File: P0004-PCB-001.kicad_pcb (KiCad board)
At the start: 2 copper layers, 63.5 x 38.5 mm, 58 parts, among them CN1 Molex 105057-0001, CN2 104031-0811, CN3 Liansheng PH--00603, CN4 Samtec FTSH-107-01-L-DV-K, CN5 M20-9990346, SW1 Khon TSB06331-090D332DA-R0500, SW2 Khon TSB06331-090D332DA-R0500, SW3 Khon TSB06331-090D332DA-R0500, SW4 Khon TSB06331-090D332DA-R0500, U1 W5500, U2 STM32H743VIT6, U3 Microchip 24AA256UIDT-I/ST, U4 INA3221AIRGV, U5 TMP102AIDRL, U6 TI LMR54410DBV

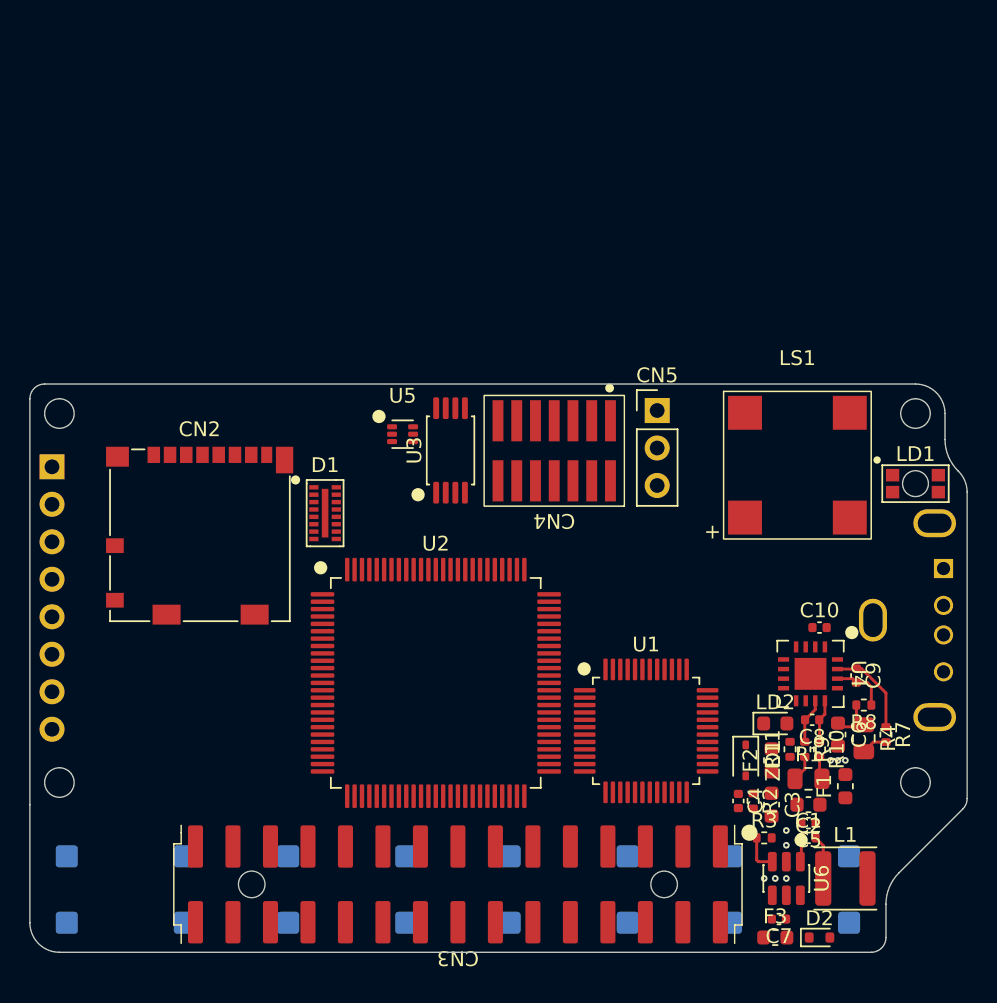
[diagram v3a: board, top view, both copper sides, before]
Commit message: added ethernet phy
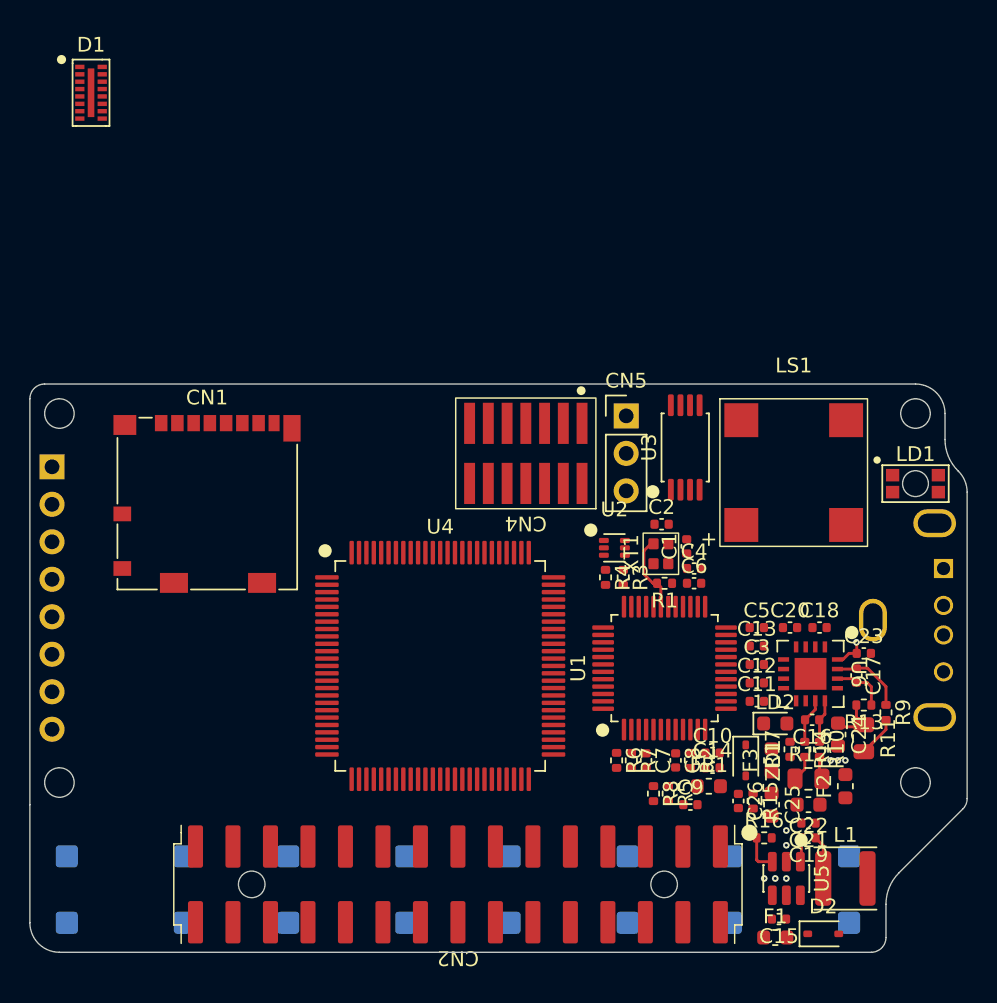
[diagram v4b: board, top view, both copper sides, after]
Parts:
- added C1: 18p, Capacitor_WUT:C_0402_1005Metric, F.Cu at (188.5, 96.5)
- added C10: 100n, Capacitor_WUT:C_0402_1005Metric, F.Cu at (190.2, 110.5)
- added C11: 100n, Capacitor_WUT:C_0402_1005Metric, F.Cu at (193.2, 107.0)
- added C12: 100n, Capacitor_WUT:C_0402_1005Metric, F.Cu at (193.2, 105.8)
- added C13: 100n, Capacitor_WUT:C_0402_1005Metric, F.Cu at (193.2, 103.2)
- added C14: 4u7, Capacitor_WUT:C_0402_1005Metric, F.Cu at (190.2, 111.5)
- added C19: 100n, Capacitor_WUT:C_0402_1005Metric, F.Cu at (196.8, 116.2)
- added C2: 18p, Capacitor_WUT:C_0402_1005Metric, F.Cu at (186.8, 95.0)
- added C20: 100n, Capacitor_WUT:C_0402_1005Metric, F.Cu at (195.5, 102.0)
- added C23: 100n, Capacitor_WUT:C_0402_1005Metric, F.Cu at (200.5, 103.8)
- added C3: 4u7, Capacitor_WUT:C_0402_1005Metric, F.Cu at (193.2, 104.5)
- added C4: 4u7, Capacitor_WUT:C_0402_1005Metric, F.Cu at (189.0, 98.0)
- added C5: 100n, Capacitor_WUT:C_0402_1005Metric, F.Cu at (193.2, 102.0)
- added C6: 100n, Capacitor_WUT:C_0402_1005Metric, F.Cu at (189.0, 99.0)
- added C7: 100n, Capacitor_WUT:C_0402_1005Metric, F.Cu at (185.8, 111.0)
- added C8: 100n, Capacitor_WUT:C_0402_1005Metric, F.Cu at (187.8, 111.0)
- added FB1: 600R, Inductor_SMD:L_0603_1608Metric, F.Cu at (190.0, 112.8)
- added R1: 1M0, Resistor_WUT:R_0402_1005Metric, F.Cu at (187.0, 99.0)
- added R2: 12k4, Resistor_WUT:R_0402_1005Metric, F.Cu at (188.8, 111.0)
- added R3: 10k, Resistor_WUT:R_0402_1005Metric, F.Cu at (184.2, 98.6)
- added R4: 10k, Resistor_WUT:R_0402_1005Metric, F.Cu at (183.0, 98.6)
- added R5: 49R9, Resistor_WUT:R_0402_1005Metric, F.Cu at (187.2, 113.2)
- added R6: 3R3, Resistor_WUT:R_0402_1005Metric, F.Cu at (183.8, 111.0)
- added R7: 3R3, Resistor_WUT:R_0402_1005Metric, F.Cu at (184.8, 111.0)
- added R8: 49R9, Resistor_WUT:R_0402_1005Metric, F.Cu at (186.2, 113.2)
- added XT1: 25MHz, Crystal_WUT:Murata_XRCGB, F.Cu at (186.8, 97.0)
- D2: footprint Diode_SMD:D_SOD-523 -> Diode_SMD:D_SOD-323
- moved D1 32.6 mm to (148.1, 65.8)
- moved U2 16.3 mm to (183.6, 96.6)
- moved U3 15.9 mm to (188.4, 89.8)
- moved C9 8.31 mm to (188.8, 114.0)
- moved U1 4.43 mm to (187.0, 104.8), turned to 90 degrees
- moved CN1 2.21 mm to (156.0, 93.6)
- moved CN5 2.13 mm to (184.4, 87.7)
- moved CN4 1.93 mm to (177.6, 90.2)
- moved R9 1.50 mm to (202.0, 107.8)
- moved U4 1.19 mm to (171.8, 104.6)
- moved LS1 0.56 mm to (195.8, 91.5)
- moved D2 0.35 mm to (197.8, 122.8)
- renumbered C7 to C15, C8 to C16, C9 to C17, C10 to C18, C5 to C21, C2 to C22, C6 to C24, C3 to C25, C4 to C26, C1 to C9, CN2 to CN1, CN3 to CN2, CN1 to CN3, F3 to F1, F1 to F2, F2 to F3, H5 to H1, H4 to H10, H8 to H11, H9 to H2, H1 to H3, H6 to H4, H10 to H5, H2 to H6, H3 to H7, H7 to H8, H11 to H9, R4 to R11, R1 to R12, R8 to R13, R9 to R14, R2 to R15, R3 to R16, R11 to R17, R7 to R9, U5 to U2, U2 to U4, U6 to U5, U4 to U6
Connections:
- net Net-(U1-AVDD-Pad11) renamed /Ethernet/PHY_VDDA
- net Net-(U4-IN3+) renamed /Power Supplies/12V_AUX_SENSE_P
- net Net-(U4-IN3-) renamed /Power Supplies/12V_AUX_SENSE_N
- C26 pad 2: Net-(U6-FB) -> 0V
- C9 pad 1: Net-(U6-CB) -> Net-(C9-Pad1)
- C9 pad 2: /Power Supplies/SW -> 0V
- R15 pad 2: Net-(U6-FB) -> Net-(U5-FB)
- R16 pad 1: Net-(U6-FB) -> Net-(U5-FB)
- U1 pad 1: unconnected-(U1-TXN-Pad1) -> Net-(U1-TXN)
- U1 pad 10: unconnected-(U1-EXRES1-Pad10) -> Net-(U1-EXRES1)
- U1 pad 14: Net-(U1-AGND-Pad14) -> 0V
- U1 pad 16: Net-(U1-AGND-Pad14) -> 0V
- U1 pad 19: Net-(U1-AGND-Pad14) -> 0V
- U1 pad 2: unconnected-(U1-TXP-Pad2) -> Net-(U1-TXP)
- U1 pad 20: unconnected-(U1-TOCAP-Pad20) -> Net-(U1-TOCAP)
- U1 pad 22: unconnected-(U1-1V2O-Pad22) -> Net-(U1-1V2O)
- U1 pad 23: unconnected-(U1-RSVD-Pad23) -> 0V
- U1 pad 25: unconnected-(U1-LINKLED-Pad25) -> /Ethernet/~{ETH_LINK_OD}
- U1 pad 27: unconnected-(U1-ACTLED-Pad27) -> /Ethernet/~{ETH_ACT_OD}
- U1 pad 28: unconnected-(U1-VDD-Pad28) -> 3V3
- U1 pad 29: unconnected-(U1-GND-Pad29) -> 0V
- U1 pad 3: Net-(U1-AGND-Pad14) -> 0V
- U1 pad 30: unconnected-(U1-XI/CLKIN-Pad30) -> Net-(U1-XI/CLKIN)
- U1 pad 31: unconnected-(U1-XO-Pad31) -> Net-(U1-XO)
- U1 pad 32: unconnected-(U1-~{SCS}-Pad32) -> /Ethernet/~{CS}
- U1 pad 33: unconnected-(U1-SCLK-Pad33) -> /Ethernet/SCLK
- U1 pad 34: unconnected-(U1-MISO-Pad34) -> /Ethernet/MISO
- U1 pad 35: unconnected-(U1-MOSI-Pad35) -> /Ethernet/MOSI
- U1 pad 36: unconnected-(U1-~{INT}-Pad36) -> /Ethernet/~{ETH_PHY_INT}
- U1 pad 37: unconnected-(U1-~{RST}-Pad37) -> /Ethernet/~{ETH_PHY_RST}
- U1 pad 43: unconnected-(U1-PMODE2-Pad43) -> 3V3
- U1 pad 44: unconnected-(U1-PMODE1-Pad44) -> 3V3
- U1 pad 45: unconnected-(U1-PMODE0-Pad45) -> 3V3
- U1 pad 48: Net-(U1-AGND-Pad14) -> 0V
- U1 pad 5: unconnected-(U1-RXN-Pad5) -> /Ethernet/ETH_RX_P
- U1 pad 6: unconnected-(U1-RXP-Pad6) -> /Ethernet/ETH_RX_N
- U1 pad 9: Net-(U1-AGND-Pad14) -> 0V
- U4 pad 10: unconnected-(U2-VSS-Pad10) -> 0V
- U4 pad 19: unconnected-(U2-VSSA-Pad19) -> 0V
- U4 pad 26: unconnected-(U2-VSS-Pad26) -> 0V
- U4 pad 49: unconnected-(U2-VSS-Pad49) -> 0V
- U4 pad 74: unconnected-(U2-VSS-Pad74) -> 0V
- U4 pad 99: unconnected-(U2-VSS-Pad99) -> 0V
- U5 pad 1: Net-(U6-CB) -> Net-(U5-CB)
- U5 pad 3: Net-(U6-FB) -> Net-(U5-FB)
- U6 pad 16: unconnected-(U4-VPU-Pad16) -> 3V3
- U6 pad 4: unconnected-(U4-VS-Pad4) -> 3V3
- U6 pad 6: unconnected-(U4-SCL-Pad6) -> /Power Supplies/SCL
- U6 pad 7: unconnected-(U4-SDA-Pad7) -> /Power Supplies/SDA
- U6 pad 9: unconnected-(U4-CRITICAL-Pad9) -> /Power Supplies/~{PWR_FAULT_OD}
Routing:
- net Net-(U1-XO): track 0.00 -> 5.27 mm
- net Net-(U6-FB): track 2.60 -> 0.00 mm
- net Net-(U5-FB): track 0.00 -> 2.60 mm
- net 3V3: track 0.00 -> 2.24 mm, vias 0 -> 1
- net Net-(F2-Pad2): track 1.77 -> 3.70 mm
- net Net-(U6-CB): track 1.74 -> 0.00 mm
- net Net-(U5-CB): track 0.00 -> 1.74 mm
- net /Power Supplies/3V3_EXPANSION_SENSE_P: track 6.30 -> 5.07 mm

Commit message: started on mcu pinout
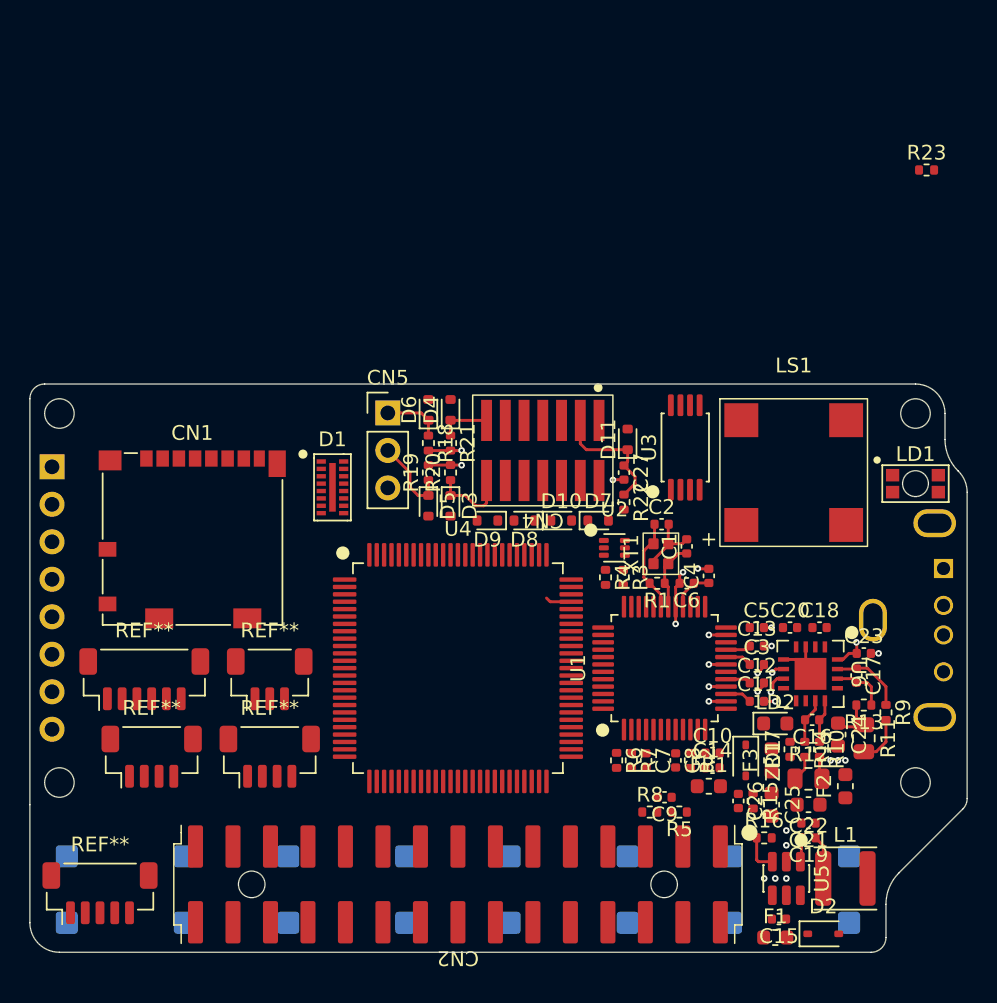
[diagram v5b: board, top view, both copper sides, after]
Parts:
- added C27: 100n, Capacitor_WUT:C_0402_1005Metric, F.Cu at (184.2, 91.5)
- added D10: 3V3, Diode_SMD:D_SOD-523, F.Cu at (180.0, 94.8)
- added D11: 3V3, Diode_SMD:D_SOD-523, F.Cu at (184.5, 89.2)
- added D3: 3V3, Diode_SMD:D_SOD-523, F.Cu at (172.5, 93.8)
- added D4: 3V3, Diode_SMD:D_SOD-523, F.Cu at (172.5, 87.2)
- added D5: 3V3, Diode_SMD:D_SOD-523, F.Cu at (171.0, 93.8)
- added D6: 3V3, Diode_SMD:D_SOD-523, F.Cu at (171.0, 87.2)
- added D7: 3V3, Diode_SMD:D_SOD-523, F.Cu at (182.5, 94.8)
- added D8: 3V3, Diode_SMD:D_SOD-523, F.Cu at (177.5, 94.8)
- added D9: 3V3, Diode_SMD:D_SOD-523, F.Cu at (175.0, 94.8)
- added R18: 100R, Resistor_WUT:R_0402_1005Metric, F.Cu at (171.0, 89.5)
- added R19: 100R, Resistor_WUT:R_0402_1005Metric, F.Cu at (171.0, 91.5)
- added R20: 100R, Resistor_WUT:R_0402_1005Metric, F.Cu at (172.5, 91.5)
- added R21: 100R, Resistor_WUT:R_0402_1005Metric, F.Cu at (172.5, 89.5)
- added R22: 1k0, Resistor_WUT:R_0402_1005Metric, F.Cu at (184.2, 93.5)
- added R23: 10k, Resistor_WUT:R_0402_1005Metric, F.Cu at (204.8, 71.0)
- added REF**: JST_SH_BM05B-SRSS-TB_1x05-1MP_P1.00mm_Vertical, Connector_JST:JST_SH_BM05B-SRSS-TB_1x05-1MP_P1.00mm_Vertical, F.Cu at (148.8, 120.0)
- added REF**: JST_SH_BM06B-SRSS-TB_1x06-1MP_P1.00mm_Vertical, Connector_JST:JST_SH_BM06B-SRSS-TB_1x06-1MP_P1.00mm_Vertical, F.Cu at (151.8, 105.5)
- added REF**: JST_SH_BM04B-SRSS-TB_1x04-1MP_P1.00mm_Vertical, Connector_JST:JST_SH_BM04B-SRSS-TB_1x04-1MP_P1.00mm_Vertical, F.Cu at (152.2, 110.8)
- added REF**: JST_SH_BM04B-SRSS-TB_1x04-1MP_P1.00mm_Vertical, Connector_JST:JST_SH_BM04B-SRSS-TB_1x04-1MP_P1.00mm_Vertical, F.Cu at (160.2, 110.8)
- added REF**: JST_SH_BM03B-SRSS-TB_1x03-1MP_P1.00mm_Vertical, Connector_JST:JST_SH_BM03B-SRSS-TB_1x03-1MP_P1.00mm_Vertical, F.Cu at (160.2, 105.5)
- moved D1 31.3 mm to (164.5, 92.5)
- moved CN5 16.2 mm to (168.2, 87.5)
- moved CN1 2.60 mm to (155.0, 96.0)
- moved C9 1.82 mm to (187.0, 113.5), turned to 180 degrees
- moved R5 1.46 mm to (188.0, 114.5), turned to 180 degrees
- moved R8 1.27 mm to (186.0, 114.5), turned to 0 degrees
- moved U4 1.21 mm to (173.0, 104.8)
- moved CN4 1.17 mm to (178.8, 90.0)
- moved C4 1.12 mm to (190.0, 98.5), turned to 90 degrees
- moved C6 0.50 mm to (188.5, 99.0), turned to 180 degrees
- moved R1 0.50 mm to (186.5, 99.0)
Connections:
- CN4 pad 12: unconnected-(CN4-T_NRST-Pad12) -> /Microcontroller/~{SWD_NRST}
- CN4 pad 13: unconnected-(CN4-T_VCP_RX-Pad13) -> Net-(CN4-T_VCP_RX)
- CN4 pad 14: unconnected-(CN4-T_VCP_TX-Pad14) -> Net-(CN4-T_VCP_TX)
- CN4 pad 3: unconnected-(CN4-T_VCC-Pad3) -> Net-(CN4-T_VCC)
- CN4 pad 4: unconnected-(CN4-T_JTMS/T_SWDIO-Pad4) -> /Microcontroller/SWD_SWDIO
- CN4 pad 5: unconnected-(CN4-GND-Pad5) -> 0V
- CN4 pad 6: unconnected-(CN4-T_JCLK/T_SWCLK-Pad6) -> /Microcontroller/SWD_SWCLK
- CN4 pad 7: unconnected-(CN4-GND-Pad7) -> 0V
- CN4 pad 8: unconnected-(CN4-T_JTDO/T_SWO-Pad8) -> /Microcontroller/SWD_SWO
- CN5 pad 1: unconnected-(CN5-Pin_1-Pad1) -> Net-(CN5-Pin_1)
- CN5 pad 2: unconnected-(CN5-Pin_2-Pad2) -> Net-(D5-K)
- CN5 pad 3: unconnected-(CN5-Pin_2-Pad3) -> 0V
- U4 pad 1: unconnected-(U4-PE2-Pad1) -> /Microcontroller/LCD_SCLK
- U4 pad 14: unconnected-(U4-NRST-Pad14) -> /Microcontroller/~{SWD_NRST}
- U4 pad 16: unconnected-(U4-PC1-Pad16) -> /Microcontroller/ETH_PHY_MOSI
- U4 pad 17: unconnected-(U4-PC2_C-Pad17) -> /Microcontroller/ETH_PHY_MISO
- U4 pad 2: unconnected-(U4-PE3-Pad2) -> /Microcontroller/LCD_BL
- U4 pad 22: unconnected-(U4-PA0-Pad22) -> /Microcontroller/UART4_TX
- U4 pad 23: unconnected-(U4-PA1-Pad23) -> /Microcontroller/UART4_RX
- U4 pad 28: unconnected-(U4-PA4-Pad28) -> /Microcontroller/~{SPI6_CS}
- U4 pad 29: unconnected-(U4-PA5-Pad29) -> /Microcontroller/SPI6_SCLK
- U4 pad 3: unconnected-(U4-PE4-Pad3) -> /Microcontroller/~{LCD_CS}
- U4 pad 30: unconnected-(U4-PA6-Pad30) -> /Microcontroller/SPI6_MISO
- U4 pad 31: unconnected-(U4-PA7-Pad31) -> /Microcontroller/SPI6_MOSI
- U4 pad 4: unconnected-(U4-PE5-Pad4) -> /Microcontroller/LCD_MISO
- U4 pad 44: unconnected-(U4-PE14-Pad44) -> /Microcontroller/<NO NET>
- U4 pad 46: unconnected-(U4-PB10-Pad46) -> /Microcontroller/I2C2_SCL
- U4 pad 47: unconnected-(U4-PB11-Pad47) -> /Microcontroller/I2C2_SDA
- U4 pad 5: unconnected-(U4-PE6-Pad5) -> /Microcontroller/LCD_MOSI
- U4 pad 51: unconnected-(U4-PB12-Pad51) -> /Microcontroller/~{ETH_PHY_CS}
- U4 pad 52: unconnected-(U4-PB13-Pad52) -> /Microcontroller/ETH_PHY_SCK
- U4 pad 53: unconnected-(U4-PB14-Pad53) -> /Microcontroller/USB_DEVICE_D_N
- U4 pad 54: unconnected-(U4-PB15-Pad54) -> /Microcontroller/USB_DEVICE_D_P
- U4 pad 59: unconnected-(U4-PD12-Pad59) -> /Microcontroller/INT_SCL
- U4 pad 60: unconnected-(U4-PD13-Pad60) -> /Microcontroller/INT_SDA
- U4 pad 65: unconnected-(U4-PC8-Pad65) -> /Microcontroller/SDMMC_D0
- U4 pad 66: unconnected-(U4-PC9-Pad66) -> /Microcontroller/SDMMC_D1
- U4 pad 67: unconnected-(U4-PA8-Pad67) -> /Microcontroller/RGB_R
- U4 pad 68: unconnected-(U4-PA9-Pad68) -> /Microcontroller/RGB_G
- U4 pad 69: unconnected-(U4-PA10-Pad69) -> /Microcontroller/RGB_B
- U4 pad 70: unconnected-(U4-PA11-Pad70) -> /Microcontroller/USB_HOST_D_N
- U4 pad 71: unconnected-(U4-PA12-Pad71) -> /Microcontroller/USB_HOST_D_P
- U4 pad 72: unconnected-(U4-PA13-Pad72) -> /Microcontroller/SWD_SWDIO
- U4 pad 76: unconnected-(U4-PA14-Pad76) -> /Microcontroller/SWD_SWCLK
- U4 pad 78: unconnected-(U4-PC10-Pad78) -> /Microcontroller/SDMMC_D2
- U4 pad 79: unconnected-(U4-PC11-Pad79) -> /Microcontroller/SDMMC_D3
- U4 pad 80: unconnected-(U4-PC12-Pad80) -> /Microcontroller/SDMMC_CLK
- U4 pad 86: unconnected-(U4-PD5-Pad86) -> /Microcontroller/DEBUG_UART_TX
- U4 pad 87: unconnected-(U4-PD6-Pad87) -> /Microcontroller/DEBUG_UART_RX
- U4 pad 89: unconnected-(U4-PB3-Pad89) -> /Microcontroller/SWD_SWO
- U4 pad 93: unconnected-(U4-PB7-Pad93) -> /Microcontroller/I2C1_SDA
- U4 pad 95: unconnected-(U4-PB8-Pad95) -> /Microcontroller/I2C1_SCL
- U4 pad 97: unconnected-(U4-PE0-Pad97) -> /Microcontroller/LCD_RST
- U4 pad 98: unconnected-(U4-PE1-Pad98) -> /Microcontroller/LCD_DC
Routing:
- net 0V: track 0.00 -> 22.4 mm, vias 8 -> 22
- net Net-(CN4-T_VCC): track 0.00 -> 8.98 mm
- net Net-(D5-K): track 0.00 -> 5.64 mm
- net Net-(CN4-T_VCP_TX): track 0.00 -> 5.37 mm
- net /Ethernet/PHY_VDDA: track 0.00 -> 5.24 mm
- net Net-(U1-XI/CLKIN): track 0.00 -> 4.65 mm
- net Net-(CN5-Pin_1): track 0.00 -> 3.99 mm
- net Net-(CN4-T_VCP_RX): track 0.00 -> 3.49 mm
- net 3V3: track 2.24 -> 5.15 mm
- net /Microcontroller/DEBUG_UART_TX: track 0.00 -> 2.25 mm, vias 0 -> 1
- net /Microcontroller/DEBUG_UART_RX: track 0.00 -> 2.25 mm, vias 0 -> 1
- net Net-(U1-TOCAP): track 0.00 -> 1.81 mm
- net /Microcontroller/SWD_SWDIO: track 0.00 -> 1.53 mm
- net /Power Supplies/SDA: track 0.00 -> 1.53 mm, vias 0 -> 1
- net Net-(U1-XO): track 5.27 -> 6.46 mm
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
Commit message: layout progress
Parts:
- removed REF**: JST_SH_BM05B-SRSS-TB_1x05-1MP_P1.00mm_Vertical, Connector_JST:JST_SH_BM05B-SRSS-TB_1x05-1MP_P1.00mm_Vertical
- removed REF**: JST_SH_BM06B-SRSS-TB_1x06-1MP_P1.00mm_Vertical, Connector_JST:JST_SH_BM06B-SRSS-TB_1x06-1MP_P1.00mm_Vertical
- removed REF** (x2): JST_SH_BM04B-SRSS-TB_1x04-1MP_P1.00mm_Vertical, Connector_JST:JST_SH_BM04B-SRSS-TB_1x04-1MP_P1.00mm_Vertical
- removed REF**: JST_SH_BM03B-SRSS-TB_1x03-1MP_P1.00mm_Vertical, Connector_JST:JST_SH_BM03B-SRSS-TB_1x03-1MP_P1.00mm_Vertical
- added D12: USBLC6-2P6, Package_TO_SOT_SMD:SOT-666, F.Cu at (201.7, 97.7)
- added LD3: Red, LED_SMD:LED_0603_1608Metric, F.Cu at (193.5, 103.8)
- added R24: 1k0, Resistor_WUT:R_0402_1005Metric, F.Cu at (191.5, 103.8)
- added R25: 10k, Resistor_WUT:R_0402_1005Metric, F.Cu at (157.2, 107.2)
- moved LS1 67.4 mm to (141.5, 131.5), turned to 90 degrees
- moved CN1 38.0 mm to (193.0, 95.5)
- moved R23 36.4 mm to (179.0, 96.8), turned to 90 degrees
- moved D1 28.8 mm to (136.2, 98.0), turned to 180 degrees
- moved U3 23.0 mm to (165.4, 90.2)
- moved C2 6.22 mm to (182.5, 99.5), turned to 90 degrees
- moved C20 5.48 mm to (200.5, 104.2)
- moved C7 5.10 mm to (180.8, 112.0), turned to 180 degrees
- moved R7 5.00 mm to (180.8, 114.0), turned to 180 degrees
- moved C4 4.51 mm to (191.5, 102.8), turned to 0 degrees
- moved C18 4.51 mm to (200.0, 105.8), turned to -90 degrees
- moved C17 4.24 mm to (197.0, 108.2), turned to 180 degrees
- moved C1 4.04 mm to (184.6, 97.5), turned to 180 degrees
- moved C6 3.88 mm to (189.5, 102.8), turned to 0 degrees
- moved C16 3.82 mm to (193.8, 106.2), turned to 90 degrees
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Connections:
- C16 pad 1: /Power Supplies/VINT_SENSE_P -> /Power Supplies/12V_AUX_SENSE_P
- C16 pad 2: /Power Supplies/VINT_SENSE_N -> /Power Supplies/12V_AUX_SENSE_N
- C17 pad 1: /Power Supplies/3V3_EXPANSION_SENSE_P -> /Power Supplies/VINT_SENSE_P
- C17 pad 2: /Power Supplies/3V3_EXPANSION_SENSE_N -> /Power Supplies/VINT_SENSE_N
- C18 pad 1: /Power Supplies/12V_AUX_SENSE_P -> /Power Supplies/3V3_EXPANSION_SENSE_P
- C18 pad 2: /Power Supplies/12V_AUX_SENSE_N -> /Power Supplies/3V3_EXPANSION_SENSE_N
- U6 pad 1: /Power Supplies/12V_AUX_SENSE_N -> /Power Supplies/3V3_EXPANSION_SENSE_N
- U6 pad 11: /Power Supplies/VINT_SENSE_N -> /Power Supplies/12V_AUX_SENSE_N
- U6 pad 12: /Power Supplies/VINT_SENSE_P -> /Power Supplies/12V_AUX_SENSE_P
- U6 pad 14: /Power Supplies/3V3_EXPANSION_SENSE_N -> /Power Supplies/VINT_SENSE_N
- U6 pad 15: /Power Supplies/3V3_EXPANSION_SENSE_P -> /Power Supplies/VINT_SENSE_P
- U6 pad 2: /Power Supplies/12V_AUX_SENSE_P -> /Power Supplies/3V3_EXPANSION_SENSE_P
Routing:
- net 0V: track 22.4 -> 3.01 mm, vias 22 -> 10
- net /Microcontroller/ETH_PHY_SCK: track 0.00 -> 10.1 mm
- net Net-(U1-XO): track 6.46 -> 1.31 mm
- net /Power Supplies/3V3_EXPANSION_SENSE_P: track 5.07 -> 0.00 mm
- net /Power Supplies/3V3_EXPANSION_SENSE_N: track 3.76 -> 0.00 mm
- net Net-(F2-Pad2): track 3.26 -> 0.00 mm
- net Net-(U1-TXP): track 0.00 -> 3.14 mm
- net Net-(U1-XI/CLKIN): track 4.65 -> 1.58 mm
- net Net-(U1-TXN): track 0.00 -> 2.18 mm
- net Net-(U1-TOCAP): track 1.81 -> 0.00 mm
- net /Ethernet/PHY_VDDA: track 5.24 -> 3.42 mm
- net /Microcontroller/~{ETH_PHY_CS}: track 0.00 -> 1.57 mm
- net /Power Supplies/VINT_SENSE_N: track 3.07 -> 1.50 mm
- net /Power Supplies/3V3_EXPANSION: track 3.36 -> 1.81 mm
- net /Microcontroller/SWD_SWDIO: track 1.53 -> 0.00 mm
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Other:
- board text added: "FUET-5020"
